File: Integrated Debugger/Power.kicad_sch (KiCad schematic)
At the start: 24 parts, among them J5 PWR, SW3 Solar Override, SW4 Target Override, U1 TPS7A2633DRVR, U5 TPS22914, U8 TPS22914

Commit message: feat: add manufacturing data
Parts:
- C1, C2: JLCPCB Part # (none) -> C76930; LCSC Part # (none) -> C76930; MPN (none) -> GRM033R60J105MEA2D
- C12: JLCPCB Part # (none) -> C76934
- J5: JLCPCB Part # (none) -> C177225
- RN1: JLCPCB Part # (none) -> C695200; LCSC Part # (none) -> C695200; MPN (none) -> YC248-JR-07100RL
- SW3, SW4: JLCPCB Part # (none) -> C2681570; LCSC Part # (none) -> C2681570; MPN (none) -> MINI MSK12CO2
- U1: JLCPCB Part # (none) -> C2876256
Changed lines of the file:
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@@
 			)
 		)
-		(property "MPN" ""
+		(property "MPN" "GRM033R60J105MEA2D"
+			(at 85.09 30.48 0)
+			(effects
+				(font
+					(size 1.27 1.27)
+				)
+				(hide yes)
+			)
+		)
+		(property "JLCPCB Part #" "C76930"
+			(at 85.09 30.48 0)
+			(effects
+				(font
+					(size 1.27 1.27)
+				)
+				(hide yes)
+			)
+		)
+		(property "LCSC Part #" "C76930"
 			(at 85.09 30.48 0)
 			(effects
@@
 			)
 		)
+		(property "JLCPCB Part #" "C2681570"
+			(at 175.26 81.28 0)
+			(effects
+				(font
+					(size 1.27 1.27)
+				)
+				(hide yes)
+			)
+		)
+		(property "LCSC Part #" "C2681570"
+			(at 175.26 81.28 0)
+			(effects
+				(font
+					(size 1.27 1.27)
+				)
+				(hide yes)
+			)
+		)
+		(property "MPN" "MINI MSK12CO2"
+			(at 175.26 81.28 0)
+			(effects
+				(font
+					(size 1.27 1.27)
+				)
+				(hide yes)
+			)
+		)
 		(pin "3"
 		)
@@
 			)
 		)
+		(property "JLCPCB Part #" "C177225"
+			(at 132.08 29.21 0)
+			(effects
+				(font
+					(size 1.27 1.27)
+				)
+				(hide yes)
+			)
+		)
 		(pin "2"
 		)
@@
 		)
 		(property "Sim.Type" ""
+			(at 76.2 30.48 0)
+			(effects
+				(font
+					(size 1.27 1.27)
+				)
+				(hide yes)
+			)
+		)
+		(property "JLCPCB Part #" "C76934"
 			(at 76.2 30.48 0)
 			(effects
@@
 			)
 		)
+		(property "JLCPCB Part #" "C695200"
+			(at 92.71 114.3 90)
+			(effects
+				(font
+					(size 1.27 1.27)
+				)
+				(hide yes)
+			)
+		)
+		(property "LCSC Part #" "C695200"
+			(at 92.71 114.3 90)
+			(effects
+				(font
+					(size 1.27 1.27)
+				)
+				(hide yes)
+			)
+		)
+		(property "MPN" "YC248-JR-07100RL"
+			(at 92.71 114.3 90)
+			(effects
+				(font
+					(size 1.27 1.27)
+				)
+				(hide yes)
+			)
+		)
 		(pin "6"
 		)
@@
 			)
 		)
+		(property "JLCPCB Part #" "C2876256"
+			(at 57.15 29.21 0)
+			(effects
+				(font
+					(size 1.27 1.27)
+				)
+				(hide yes)
+			)
+		)
 		(pin "2"
 		)
@@
 			)
 		)
+		(property "JLCPCB Part #" "C2681570"
+			(at 142.24 81.28 0)
+			(effects
+				(font
+					(size 1.27 1.27)
+				)
+				(hide yes)
+			)
+		)
+		(property "LCSC Part #" "C2681570"
+			(at 142.24 81.28 0)
+			(effects
+				(font
+					(size 1.27 1.27)
+				)
+				(hide yes)
+			)
+		)
+		(property "MPN" "MINI MSK12CO2"
+			(at 142.24 81.28 0)
+			(effects
+				(font
+					(size 1.27 1.27)
+				)
+				(hide yes)
+			)
+		)
 		(pin "3"
 		)
@@
 			)
 		)
-		(property "MPN" ""
+		(property "MPN" "GRM033R60J105MEA2D"
 			(at 35.56 30.48 0)
 			(effects
+				(font
+					(size 1.27 1.27)
+				)
+				(hide yes)
+			)
+		)
+		(property "JLCPCB Part #" "C76930"
+			(at 35.56 30.48 0)
+			(effects
+				(font
+					(size 1.27 1.27)
+				)
+				(hide yes)
+			)
+		)
+		(property "LCSC Part #" "C76930"
+			(at 35.56 30.48 0)
+			(effects

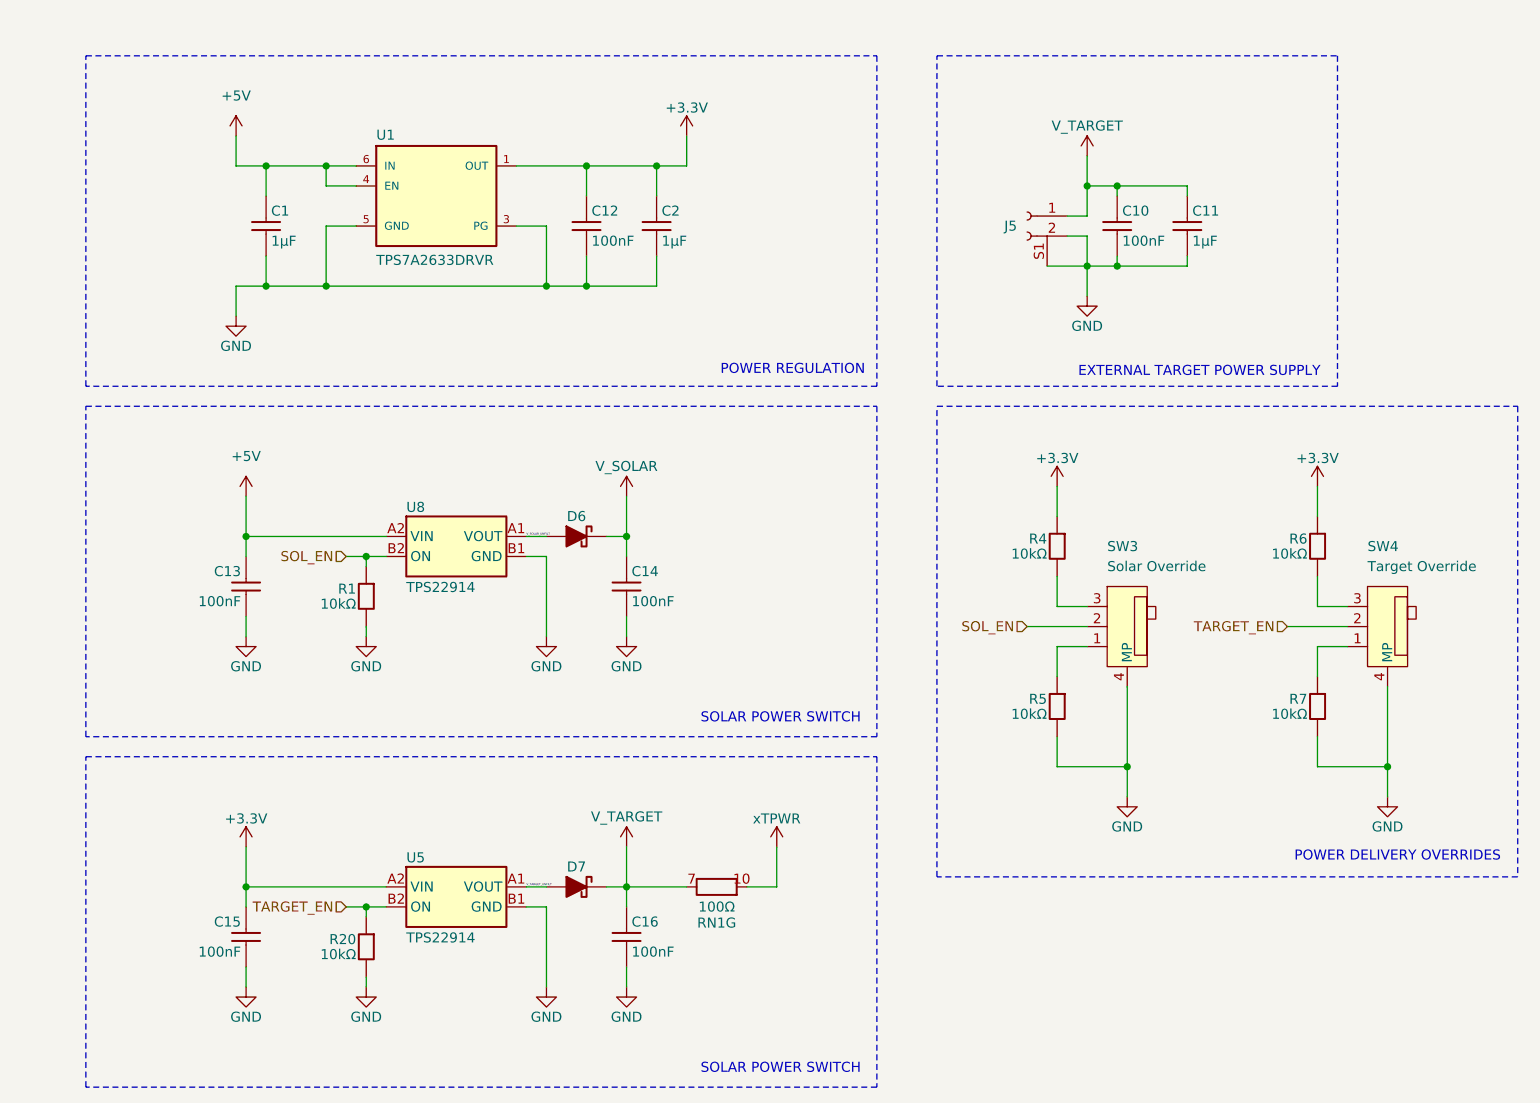
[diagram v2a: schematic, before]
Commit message: Schematic consistency improvements
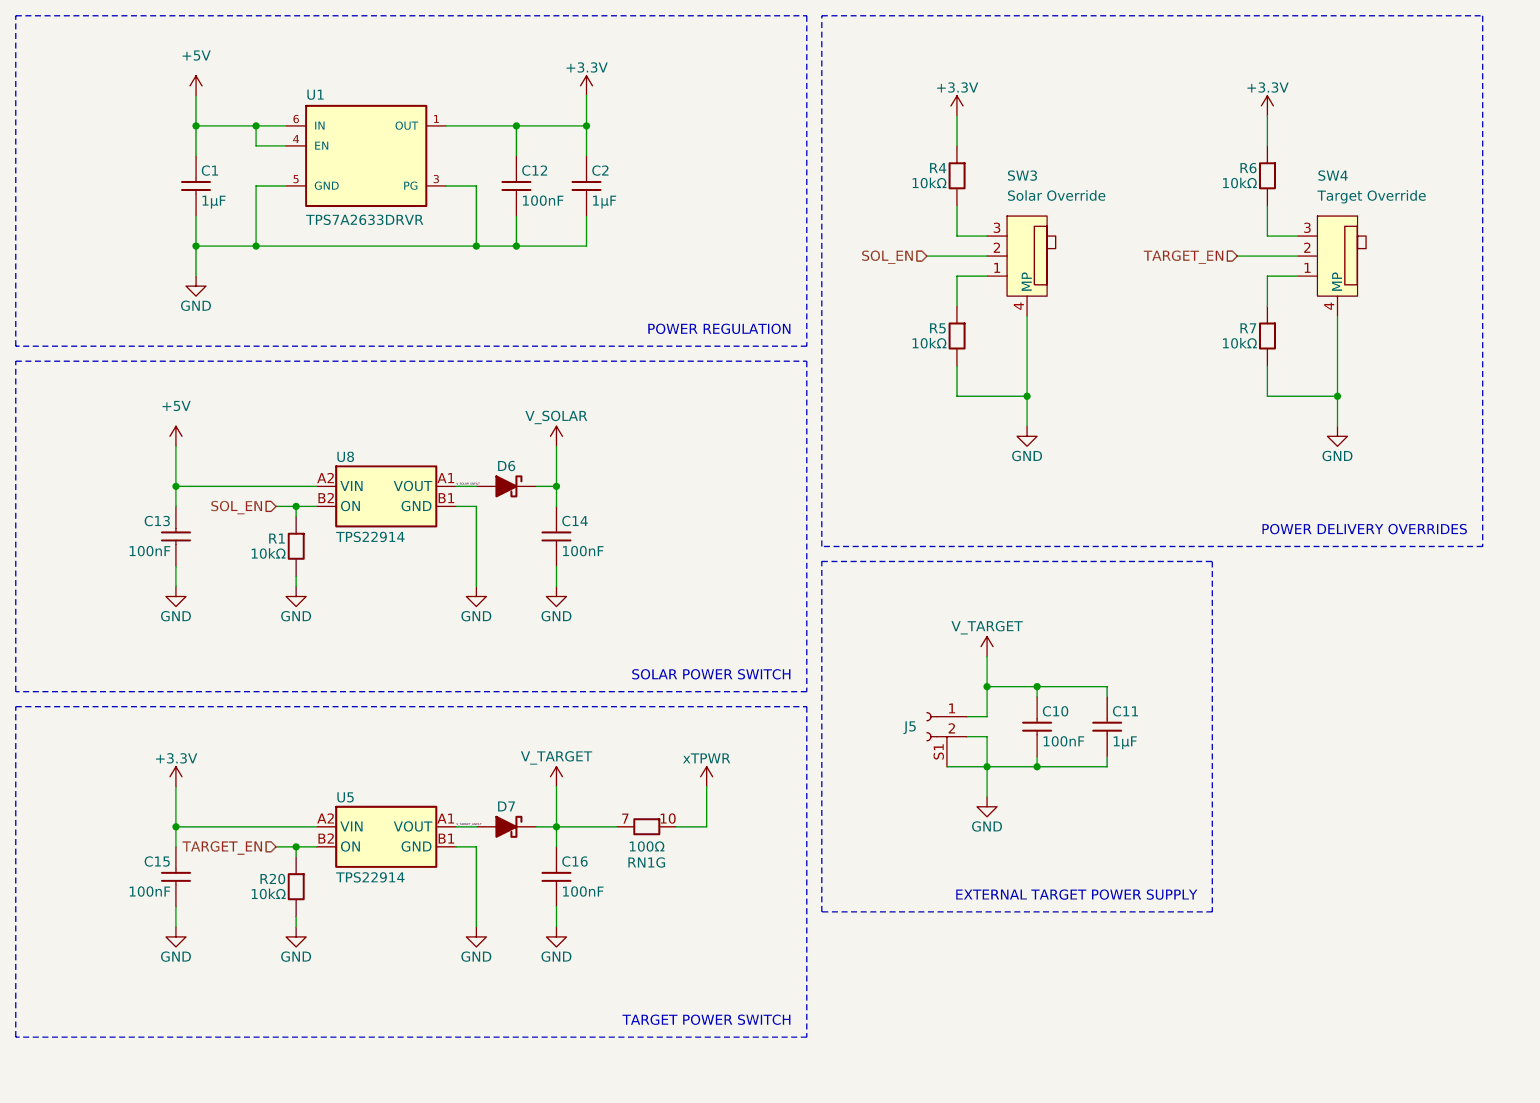
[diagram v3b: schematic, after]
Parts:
- D6, D7: symbol Picoballoon Passives:Schottky Diode -> Picoballoon Passives:Schottky diode
- RN1: symbol Picoballoon Passives:R_Pack08_Split -> Picoballoon Passives:Resistor array 8
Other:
- note added: "TARGET POWER SWITCH"
- moved on the sheet: C1, C10, C11, C12, C13, C14, C15, C16, C2, D6, D7, J5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

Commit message: PCB improvements
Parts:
- removed D7: PMEG3005EL,315, Picoballoon Passives:Diode SOD-882, symbol Picoballoon Passives:Schottky diode
- renumbered C1 to C10, C12 to C11, C14 to C12, C16 to C13, C2 to C14, C10 to C15, C11 to C16, C13 to C8, C15 to C9, D6 to D5, R1 to R13, R20 to R14, R4 to R15, R5 to R16, R6 to R17, R7 to R18, U1 to U4, U8 to U5, U5 to U6
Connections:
- net V_TARGET_UNFILT is gone; now on net V_TARGET: U6.A1 (VOUT)
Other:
- title: Power -> Power supply
- moved on the sheet: C13, C9, RN1G

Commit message: Update BOM
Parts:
- C10, C14, C16: LCSC Part # C76930 -> C335102; MPN GRM033R60J105MEA2D -> GRM033R61C105ME15D
- C11, C15: LCSC Part # C76934 -> C181043; MPN GRM033R61A104KE15D -> GRM033R6YA104KE14D
- C12: renamed from C13; LCSC Part # C76934 -> C181043; MPN GRM033R61A104KE15D -> GRM033R6YA104KE14D
- C13: renamed from C12; LCSC Part # C76934 -> C181043; MPN GRM033R61A104KE15D -> GRM033R6YA104KE14D
- C8: renamed from C9; LCSC Part # C76934 -> C181043; MPN GRM033R61A104KE15D -> GRM033R6YA104KE14D
- C9: renamed from C8; LCSC Part # C76934 -> C181043; MPN GRM033R61A104KE15D -> GRM033R6YA104KE14D
- D5: value PMEG3005EL,315 -> CTS520,L3F(T; LCSC Part # C282565 -> C2847407; MPN PMEG3005EL,315 -> CTS520,L3F(T
- renumbered R13 to R14, R14 to R15, R15 to R16, R16 to R17, R17 to R18, R18 to R19

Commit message: Change diode
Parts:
- D5: footprint Picoballoon Passives:Diode SOD-882 -> Picoballoon Passives:Diode SOD-323F; JLCPCB Part # C282565 -> (none); LCSC Part # C2847407 -> C841776; MPN CTS520,L3F(T -> PMEG2020EJ,115
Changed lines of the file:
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@@
 			)
 		)
-		(property "Footprint" "Picoballoon Passives:Diode SOD-882"
+		(property "Footprint" "Picoballoon Passives:Diode SOD-323F"
 			(at 66.04 63.5 0)
 			(effects
@@
 			)
 		)
-		(property "MPN" "CTS520,L3F(T"
+		(property "MPN" "PMEG2020EJ,115"
 			(at 66.04 63.5 0)
 			(effects
@@
 			)
 		)
-		(property "JLCPCB Part #" "C282565"
+		(property "LCSC Part #" "C841776"
 			(at 66.04 63.5 0)
 			(effects
-				(font
-					(size 1.27 1.27)
-				)
-				(hide yes)
-			)
-		)
-		(property "LCSC Part #" "C2847407"
-			(at 66.04 63.5 0)
-			(effects

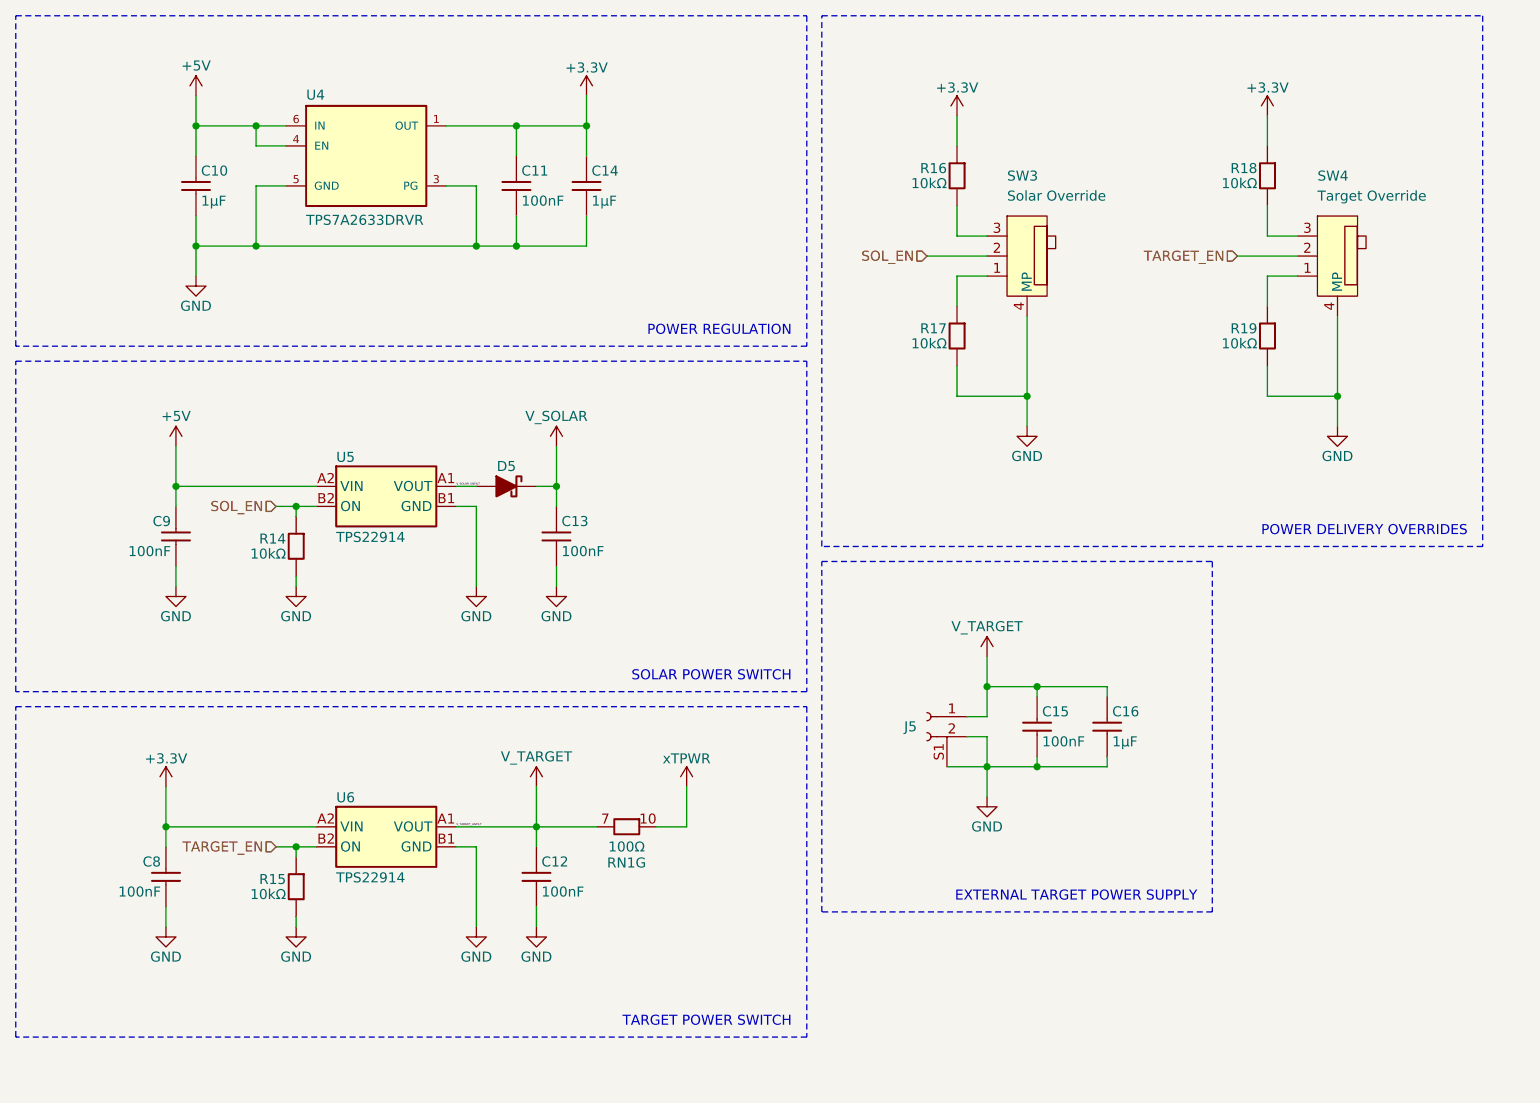
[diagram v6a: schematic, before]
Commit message: feat: fix debugger bugs & impl. auxiliary power - 869b0p9f3
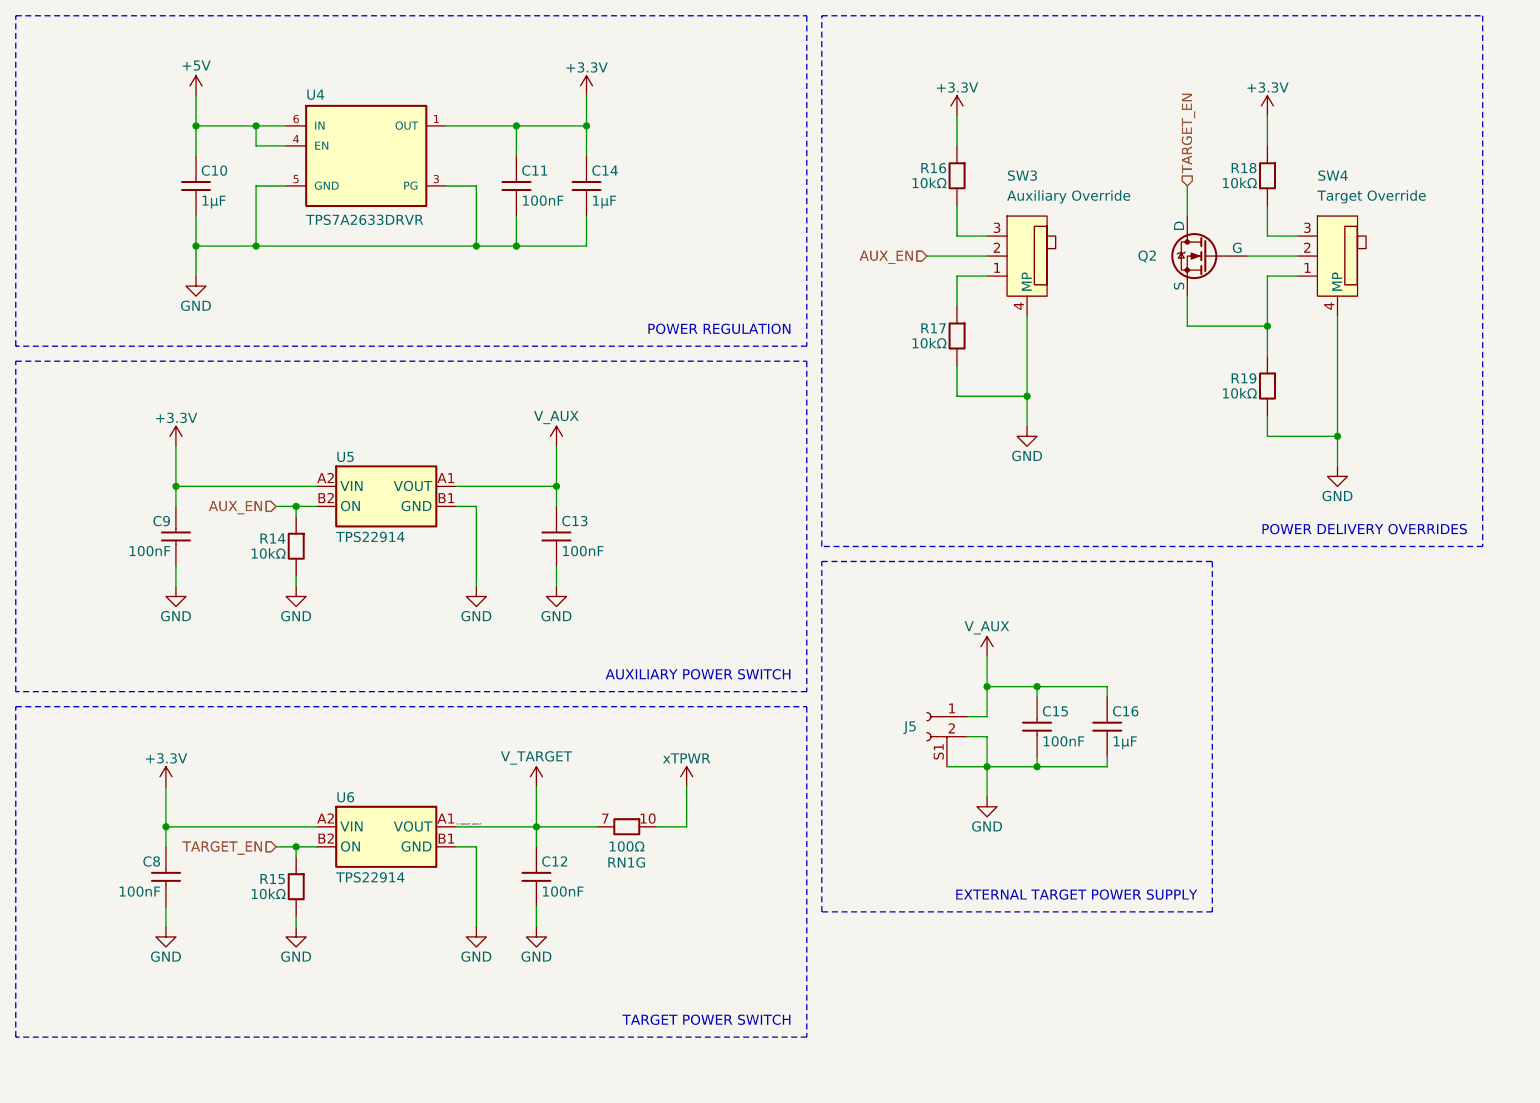
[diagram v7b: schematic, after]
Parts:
- removed D5: CTS520,L3F(T, Picoballoon Passives:Diode SOD-323F, symbol Picoballoon Passives:Schottky diode
- added Q2: Generic N-MOSFET, PCM_Picoballoon ICs:PICOSTAR-3, symbol Picoballoon ICs:Generic N-MOSFET
- SW3: value Solar Override -> Auxiliary Override
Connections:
- net V_SOLAR_UNFILT is gone; now on net V_AUX: U5.A1 (VOUT)
- net +3.3V: now also C9.1, U5.A2 (VIN)
- net +5V: no longer C9.1, U5.A2 (VIN)
- net TARGET_EN: now also Q2.3 (D); no longer SW4.2
- net V_TARGET: no longer C15.1, C16.1, J5.1 (Pin_1)
- net at R19.1, SW4.1: now also Q2.2 (S)
- net SOL_EN renamed AUX_EN
- net V_SOLAR renamed V_AUX
- net V_AUX: now also C15.1, C16.1, J5.1 (Pin_1)
- new net: Q2.1 (G), SW4.2
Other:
- note added: "AUXILIARY POWER SWITCH"
- note removed: "SOLAR POWER SWITCH"
- moved on the sheet: R19

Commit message: chore: debugger add mosfet mfr details
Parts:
- Q2: JLCPCB Part # (none) -> C179868; LCSC Part # (none) -> C179868; MPN (none) -> CSD13381F4
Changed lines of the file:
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@@
+			)
+		)
+		(property "JLCPCB Part #" "C179868"
+			(at 154.94 34.29 0)
+			(effects
+				(font
+					(size 1.27 1.27)
+				)
+				(hide yes)
+			)
+		)
+		(property "LCSC Part #" "C179868"
+			(at 154.94 34.29 0)
+			(effects
+				(font
+					(size 1.27 1.27)
+				)
+				(hide yes)
+			)
+		)
+		(property "MPN" "CSD13381F4"
+			(at 154.94 34.29 0)
+			(effects
+				(font
+					(size 1.27 1.27)
+				)
+				(hide yes)
 			)
 		)
